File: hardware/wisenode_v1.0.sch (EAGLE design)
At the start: 32 parts, among them J1 AUDIO-JACK2PTH, J2 M04X2, Q1 G2XX3---PW20, Q4 32.768 kHz, U1 MIC5025-3.3, X1 USBSMD

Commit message: schematic .png
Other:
- note added: "."
- note added: "NRF24L01+"
- moved on the sheet: C1, C2, C3, C4, C6, C8, J3, J4, Q4, R10, R3, R4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

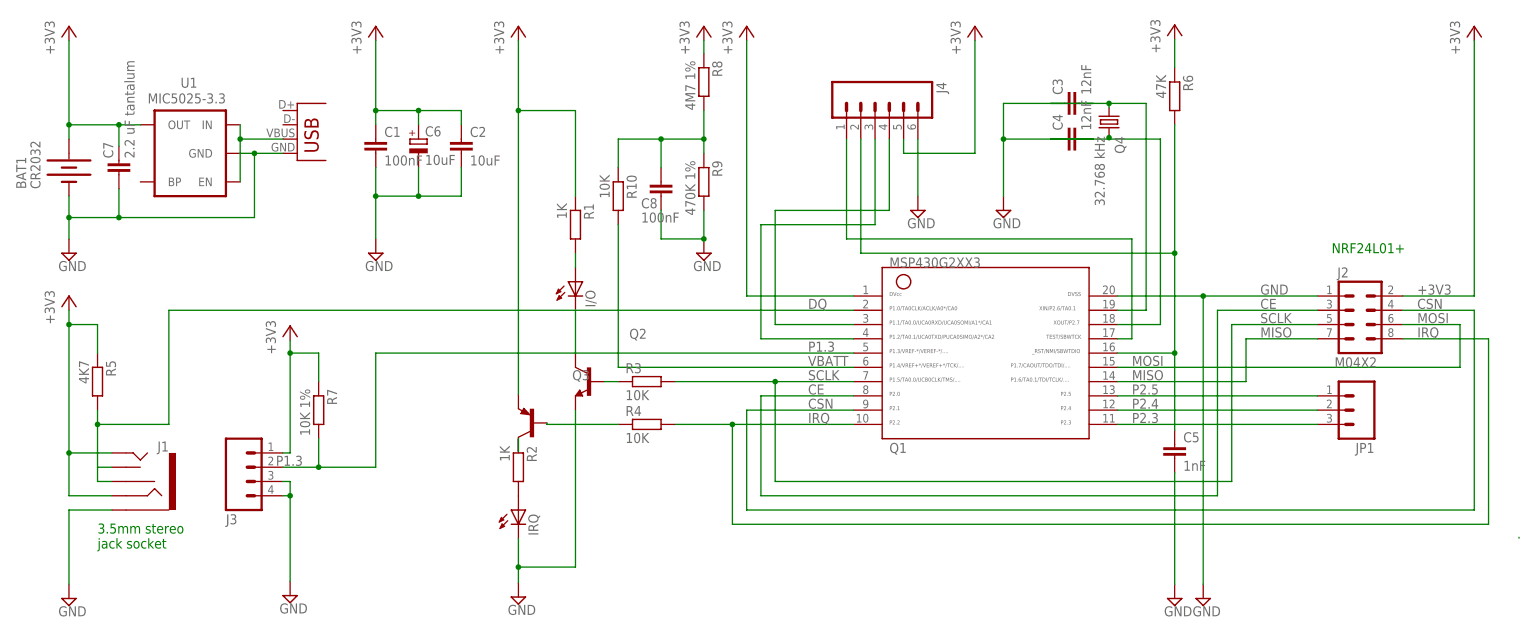
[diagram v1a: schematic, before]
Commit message: BAT54A diode avoid charging battery
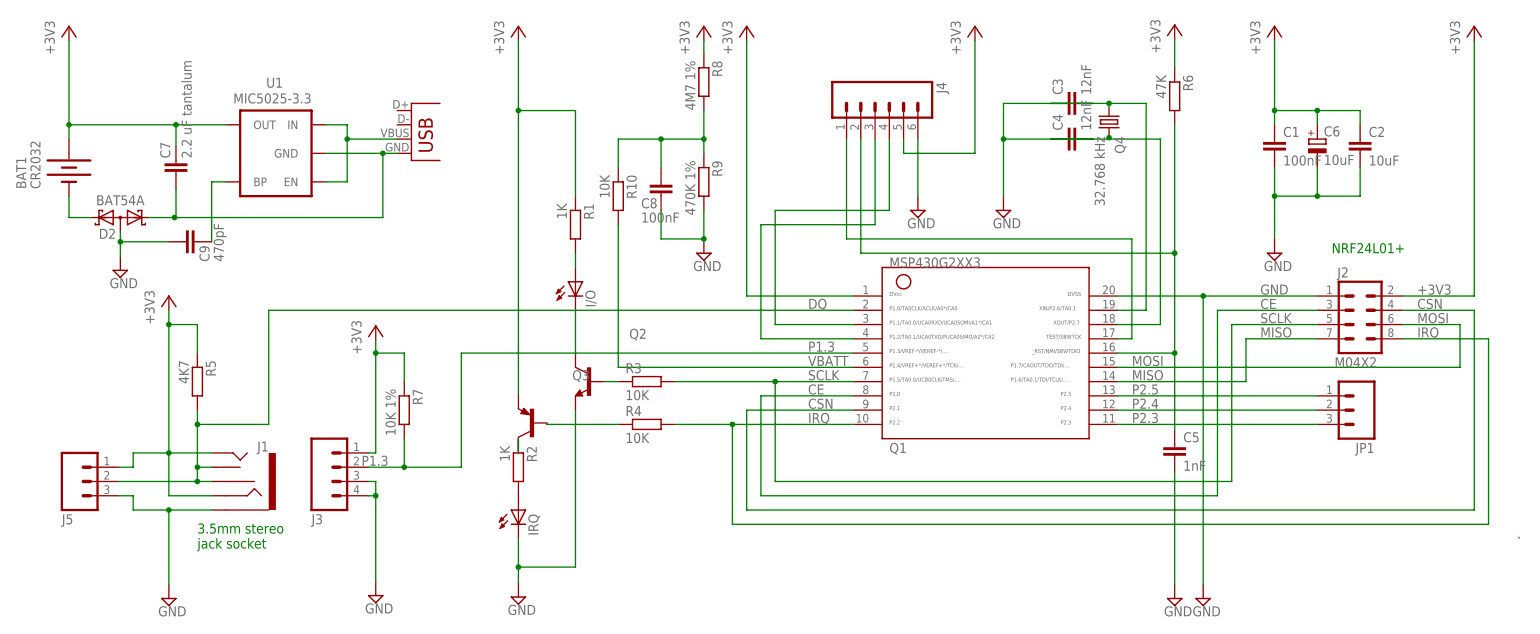
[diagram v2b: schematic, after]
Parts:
- added C9: 470pF, resistor:C-EUC0805
- added D2: BAT54A, diode:BAT54A
- added J5: (no value), SparkFun:M03PTH
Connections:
- new net N$11: C7.2, D2.K1, U1.GND, X1.GND
- new net N$13: BAT1.-, D2.K2
- new net N$15: C9.2, U1.BP
- net +3V3: now also J5.1
- net DQ: now also J5.2
- net GND: now also C9.1, D2.AA, J5.3; no longer BAT1.-, C7.2, U1.GND, X1.GND
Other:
- moved on the sheet: C1, C2, C6, C7, J1, J3, R5, R7, U1

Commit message: changed LEDs, added push button
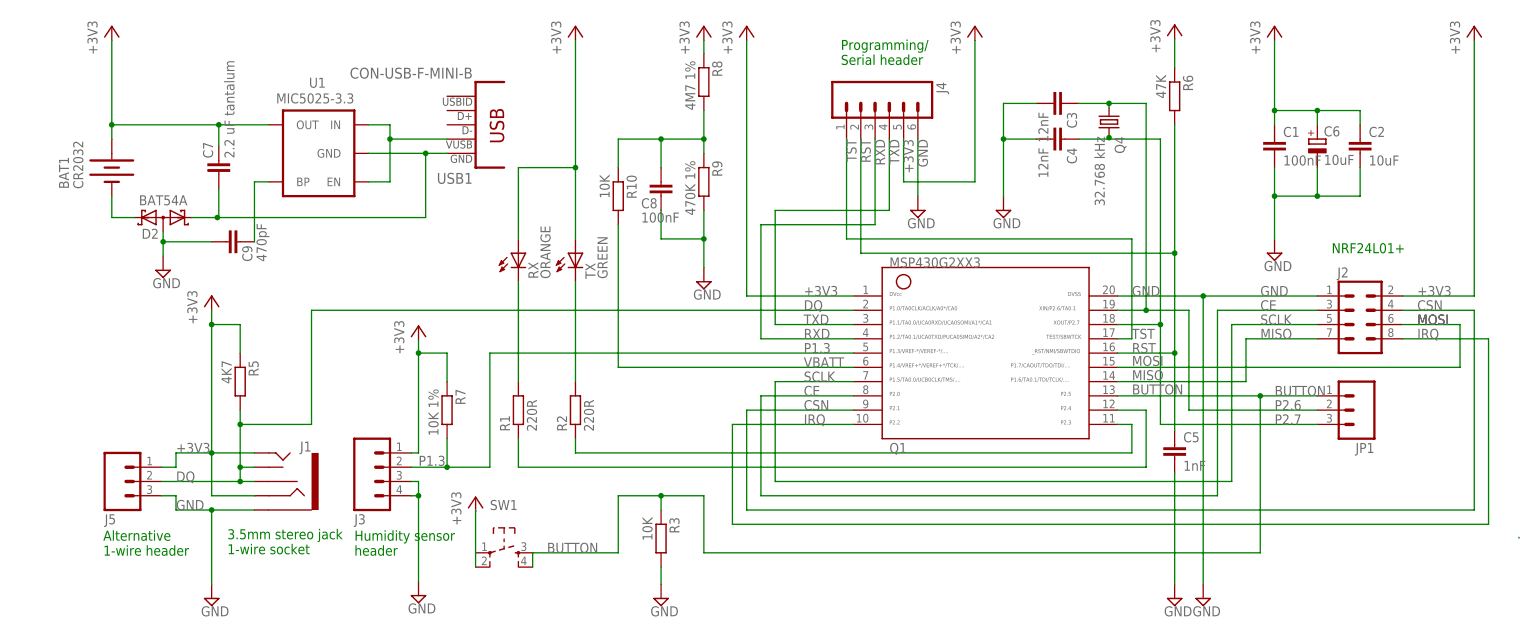
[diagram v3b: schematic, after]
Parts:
- removed I/O, IRQ: (no value), led:LEDCHIPLED_0805
- removed Q2: (no value), transistor:BC847C-NPN-SOT23-BEC
- removed Q3: (no value), transistor-neu-to92:BC856B-PNP-SOT23-BEC
- removed R4: 10K, resistor:R-EU_M0805
- removed X1: USBSMD, SparkFun:USBSMD
- added RX: ORANGE, led:LEDCHIPLED_0805
- added SW1: (no value), dp_devices:SW_TACT_4P
- added TX: GREEN, led:LEDCHIPLED_0805
- added USB1: CON-USB-F-MINI-B, dp_devices:CON-USB-F-MINI-B
- R1, R2: value 1K -> 220R
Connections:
- net N$14 renamed TXD
- net N$5 renamed RST
- net N$9 renamed TST
- net P24 renamed RXD
- removed net N$10: Q3.B, R4.1
- removed net N$4: C3.1, Q1.19, Q4.1
- removed net N$6: I/O.C, Q2.C
- removed net N$7: Q2.B, R3.1
- removed net N$8: Q3.C, R2.1
- removed net P2.3: JP1.3, Q1.11
- removed net P2.4: JP1.2, Q1.12
- removed net P2.5: JP1.1, Q1.13
- new net BUTTON: JP1.1, Q1.13, R3.1, SW1.3, SW1.4
- new net N$5: Q1.12, R1.1
- new net P2.6: C3.1, JP1.2, Q1.19, Q4.1
- new net P2.7: C4.1, JP1.3, Q1.18, Q4.2
- net +3V3: now also RX.A, SW1.1, SW1.2, TX.A; no longer Q3.E, R1.1
- net GND: now also R3.2; no longer IRQ.C, Q2.E
- net IRQ: no longer R4.2
- net N$1: now also R2.2, TX.C; no longer I/O.A, R1.2
- net N$11: now also USB1USB.GND; no longer X1.GND
- net N$12: now also USB1USB.VUSB; no longer X1.VBUS
- net N$2: now also R1.2, RX.C; no longer IRQ.A, R2.2
- net N$3: now also Q1.11, R2.1; no longer C4.1, Q1.18, Q4.2
- net SCLK: no longer R3.2
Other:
- note added: "3.5mm stereo jack 1-wire socket"
- note added: "Alternative 1-wire header"
- note added: "Humidity sensor header"
- note added: "Programming/ Serial header"
- note removed: "3.5mm stereo jack socket"
- moved on the sheet: BAT1, C3, C4, C7, C9, D2, J1, J3, J5, R1, R2, R3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
